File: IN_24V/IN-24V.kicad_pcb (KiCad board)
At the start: 2 copper layers, 5 x 34 mm, 12 parts, among them U1 SN74LVC1T45DCK

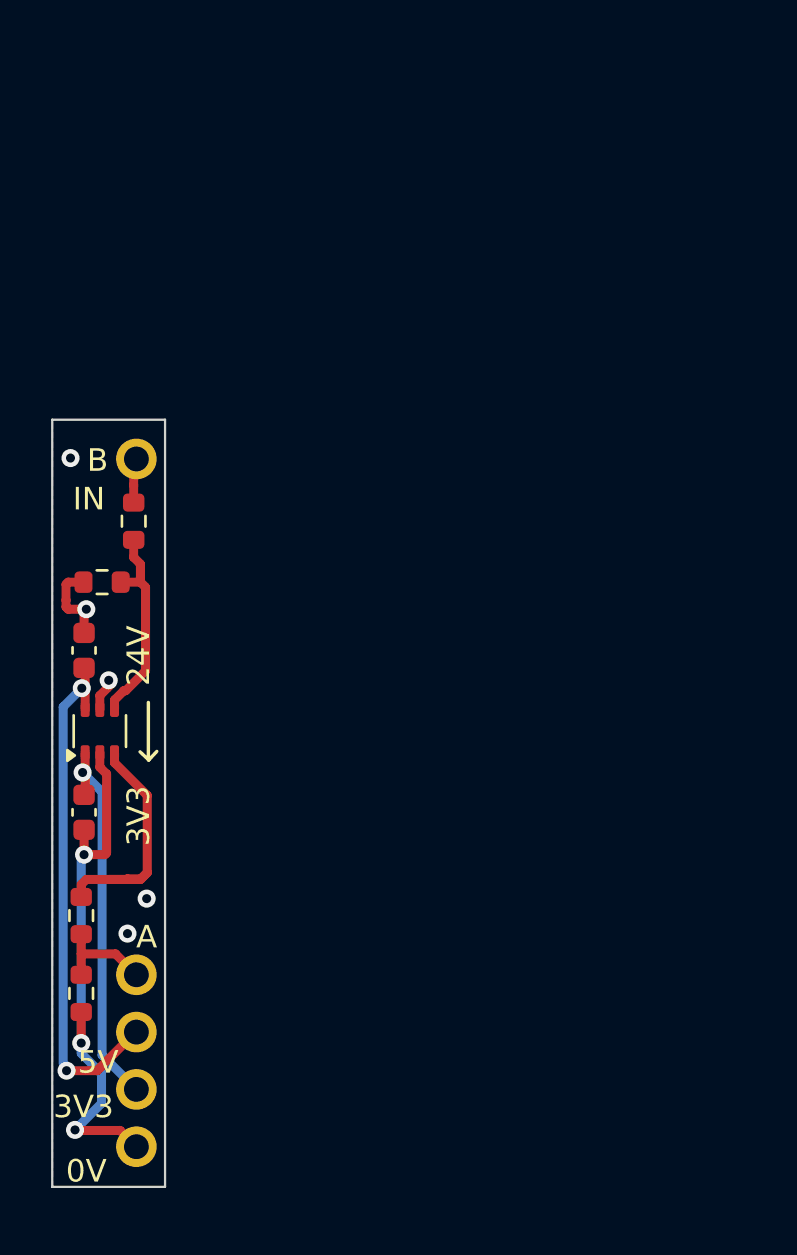
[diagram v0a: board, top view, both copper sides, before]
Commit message: IN-24V passage à opto et nouveau format
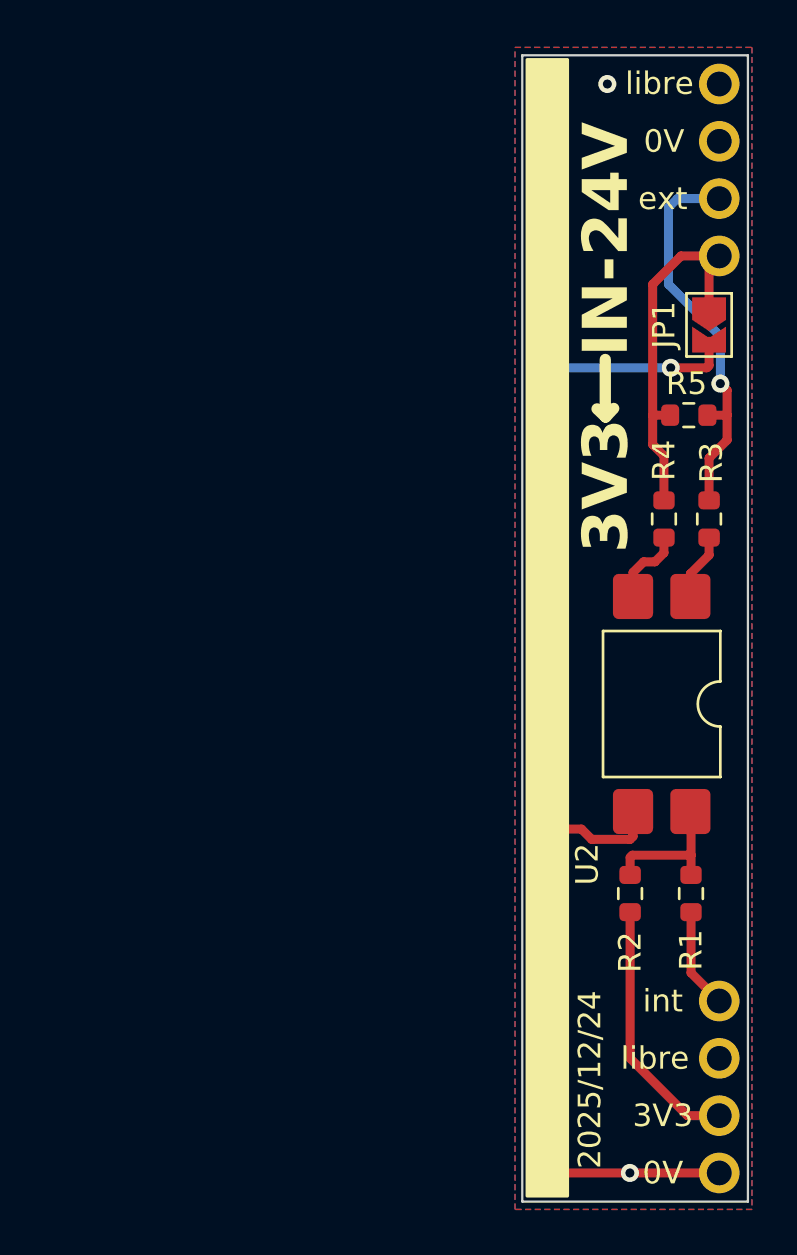
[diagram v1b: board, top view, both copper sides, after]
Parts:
- removed C1, C2: 100nF 50V X7R, Capacitor_SMD:C_0603_1608Metric
- removed R6: 10k, Resistor_SMD:R_0603_1608Metric
- removed TP5: TestPoint, Chimere_comps:Pastille
- removed U1: SN74LVC1T45DCK, Package_TO_SOT_SMD:SOT-363_SC-70-6
- added JP1: SolderJumper_2_Open, Jumper:SolderJumper-2_P1.3mm_Open_TrianglePad1.0x1.5mm, F.Cu at (274.3, 60.1)
- added R3: 2k2, Resistor_SMD:R_0603_1608Metric, F.Cu at (274.3, 68.7)
- added R4: 2k2, Resistor_SMD:R_0603_1608Metric, F.Cu at (272.3, 68.7)
- added TP17: TestPoint, Chimere_comps:Pastille, F.Cu at (274.8, 57.0)
- added TP18: TestPoint, Chimere_comps:Pastille, F.Cu at (274.8, 54.5)
- added TP19: TestPoint, Chimere_comps:Pastille, F.Cu at (274.8, 52.0)
- added TP20: TestPoint, Chimere_comps:Pastille, F.Cu at (274.8, 49.4)
- added U2: LTV-817S-TA1-C, Package_DIP:SMDIP-4_W9.53mm, F.Cu at (272.2, 76.9)
- R1: value 100k -> 1k
- R2: value 1k -> 10k
- R5: value 2k2 -> 100k
- moved TP1 40.8 mm to (274.8, 97.7)
- moved R1 27.4 mm to (273.5, 85.3), turned to 90 degrees
- moved R5 27.0 mm to (273.4, 64.1)
- moved TP2 26.6 mm to (274.8, 95.1)
- moved TP4 26.1 mm to (274.8, 90.1)
- moved TP3 25.9 mm to (274.8, 92.6)
- moved R2 24.3 mm to (270.8, 85.3), turned to -90 degrees
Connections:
- R1 pad 1: /IN_i -> /int
- R1 pad 2: /GND -> Net-(R1-Pad2)
- R2 pad 1: /IN_i -> Net-(R1-Pad2)
- R2 pad 2: Net-(U1-A) -> /3V3
- R5 pad 1: Net-(U1-B) -> /ext
- R5 pad 2: /GND -> /ext_ref
- TP1 pad 1: /IN -> /0V
- TP2 pad 1: /IN_i -> /3V3
- TP3 pad 1: /5V -> unconnected-(TP3-Pad1)
- TP4 pad 1: /3V3 -> /int
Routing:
- net /GND: track 29.7 -> 0.00 mm, vias 8 -> 0
- net /5V: track 22.7 -> 0.00 mm, vias 2 -> 0
- net /0V: track 0.00 -> 20.7 mm, vias 0 -> 23
- net /ext: track 0.00 -> 17.7 mm, vias 0 -> 1
- net /ext_ref: track 0.00 -> 16.5 mm
- net Net-(U1-A): track 11.5 -> 0.00 mm
- net Net-(U1-B): track 9.23 -> 0.00 mm
- net Net-(R1-Pad2): track 0.00 -> 6.34 mm
- net /3V3: track 17.0 -> 11.5 mm, vias 1 -> 0
- net /IN_i: track 4.63 -> 0.00 mm
- net /int: track 0.00 -> 4.46 mm
- net Net-(R4-Pad1): track 0.00 -> 3.47 mm
- net Net-(R3-Pad1): track 0.00 -> 2.95 mm
- net /IN: track 1.81 -> 0.00 mm
- added copper zone on B.Cu, net /0V
- added copper zone on F.Cu, net /0V
- removed copper zone on B.Cu, net /GND
- removed copper zone on F.Cu, net /GND
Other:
- board size 5 x 34 mm -> 10 x 50.8 mm
- board text added: "2025/12/24"
- board text added: "EXT_REF = 0V si JP1 brasé"
- board text added: "IN-24V"
- board text added: "ext"
- board text added: "int"
- board text added: "libre"
- board text removed: "2024/12/02"
- board text removed: "24V"
- board text removed: "5V"
- board text removed: "A"
- board text removed: "B"
- board text removed: "IN"
